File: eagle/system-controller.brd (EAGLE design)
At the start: 99 x 100 mm, 222 parts, among them IC1 TS4100, Q1 MOSFET-P-N-PAIR, Q10 MOSFET-P-N-PAIR, Q11 MOSFET-P-N-PAIR, Q12 MOSFET-P-N-PAIR, Q13 MOSFET-P-N-PAIR, Q14 MOSFET-P-N-PAIR, Q15 MOSFET-P-N-PAIR, Q16 MOSFET-P-N-PAIR, Q17 MOSFET-P-N-PAIR, Q18 MOSFET-P-N-PAIR, Q19 MOSFET-P-N-PAIR, Q2 MOSFET-P-N-PAIR, Q3 DNP/NTR4101P, Q4 DNP/NTR4101P, Q5 DNP/NTR4101P, Q6 DNP/NTR4101P, Q7 MOSFET-P-N-PAIR, Q8 MOSFET-P-N-PAIR, Q9 MOSFET-P-N-PAIR, SW1 TPS25944LRVCRWQFN-20-3X4, SW2 TPS25944LRVCRWQFN-20-3X4, SW3 TPS25944LRVCRWQFN-20-3X4, SW4 TPS25944LRVCRWQFN-20-3X4, SW5 TPS25944LRVCRWQFN-20-3X4, SW6 TPS25944LRVCRWQFN-20-3X4, SW7 TPS25944LRVCRWQFN-20-3X4, SW8 TPS25944LRVCRWQFN-20-3X4, U1 MEGA128-A, X1 8 MHz CRYSTAL-ABRACON-ABM3-SMD

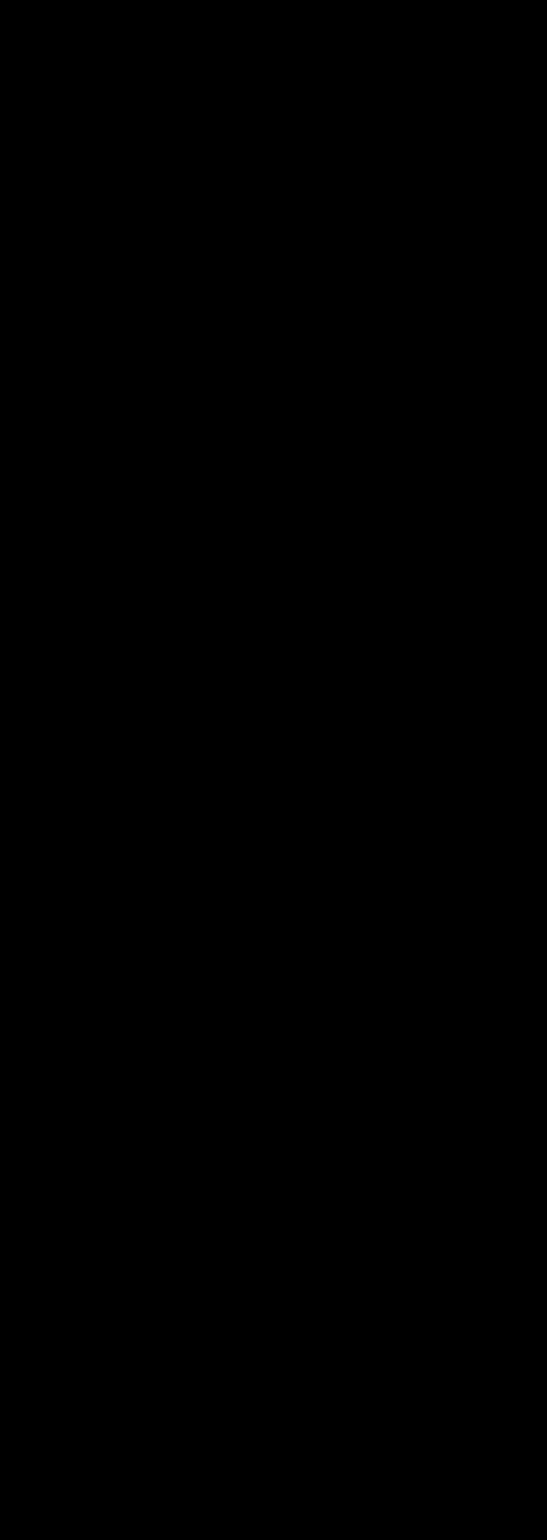
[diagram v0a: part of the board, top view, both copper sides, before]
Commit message: added the remaining test points
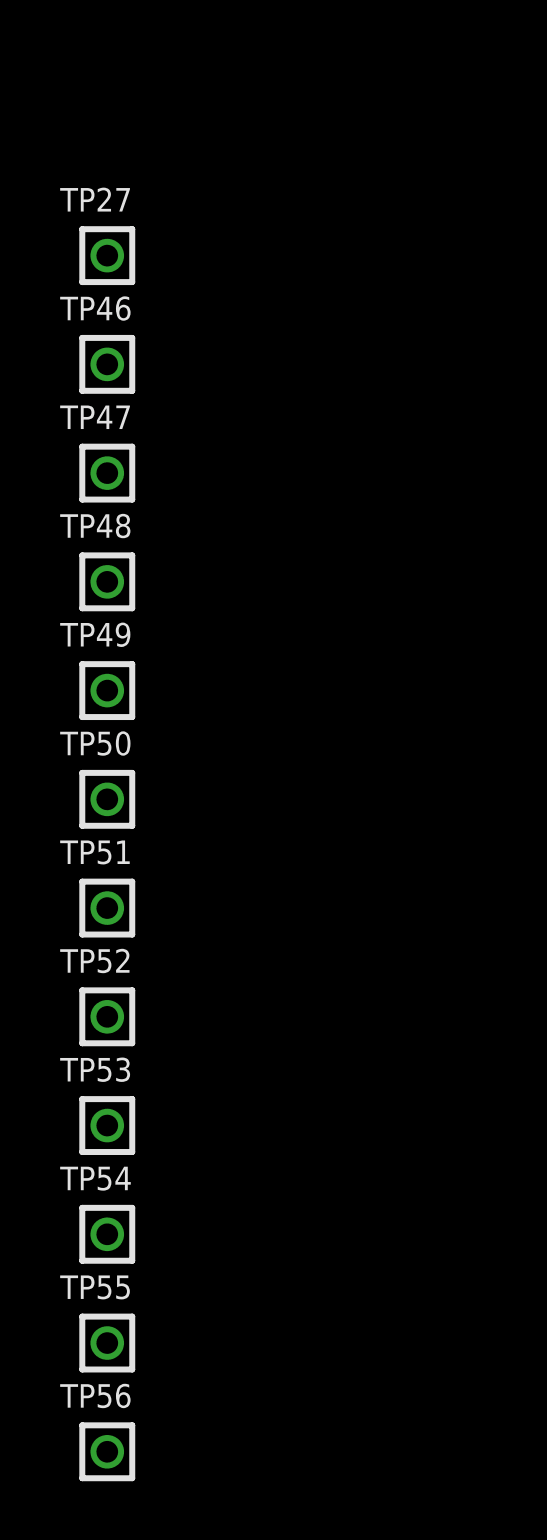
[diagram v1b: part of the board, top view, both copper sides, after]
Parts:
- added TP27, TP46, TP47, TP48, TP49, TP50, TP51, TP52, TP53, TP54, TP55, TP56: TEST-POINT, Tova:2MM-TEST-POINT
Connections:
- net N$104: now also TP56.1
- net N$27: now also TP46.1
- net N$28: now also TP27.1
- net N$34: now also TP47.1
- net N$35: now also TP49.1
- net N$37: now also TP48.1
- net N$39: now also TP55.1
- net N$40: now also TP54.1
- net N$41: now also TP53.1
- net N$42: now also TP52.1
- net N$43: now also TP51.1
- net N$44: now also TP50.1
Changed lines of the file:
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@@
 <?xml version="1.0" encoding="utf-8"?>
 <!DOCTYPE eagle SYSTEM "eagle.dtd">
-<eagle version="7.3.0">
+<eagle version="7.5.0">
 <drawing>
 <settings>
@@
 <attribute name="DPN" value="SSC53L-E3/57TGICT-ND" x="102.4" y="-12" size="1.778" layer="27" display="off"/>
 </element>
+<element name="TP27" library="Tova" package="2MM-TEST-POINT" value="TEST-POINT" x="-6.7" y="-19.3"/>
+<element name="TP46" library="Tova" package="2MM-TEST-POINT" value="TEST-POINT" x="-6.7" y="-23"/>
+<element name="TP47" library="Tova" package="2MM-TEST-POINT" value="TEST-POINT" x="-6.7" y="-26.7"/>
+<element name="TP48" library="Tova" package="2MM-TEST-POINT" value="TEST-POINT" x="-6.7" y="-30.4"/>
+<element name="TP49" library="Tova" package="2MM-TEST-POINT" value="TEST-POINT" x="-6.7" y="-34.1"/>
+<element name="TP50" library="Tova" package="2MM-TEST-POINT" value="TEST-POINT" x="-6.7" y="-37.8"/>
+<element name="TP51" library="Tova" package="2MM-TEST-POINT" value="TEST-POINT" x="-6.7" y="-41.5"/>
+<element name="TP52" library="Tova" package="2MM-TEST-POINT" value="TEST-POINT" x="-6.7" y="-45.2"/>
+<element name="TP53" library="Tova" package="2MM-TEST-POINT" value="TEST-POINT" x="-6.7" y="-48.9"/>
+<element name="TP54" library="Tova" package="2MM-TEST-POINT" value="TEST-POINT" x="-6.7" y="-52.6"/>
+<element name="TP55" library="Tova" package="2MM-TEST-POINT" value="TEST-POINT" x="-6.7" y="-56.3"/>
+<element name="TP56" library="Tova" package="2MM-TEST-POINT" value="TEST-POINT" x="-6.7" y="-60"/>
 </elements>
 <signals>
@@
 <signal name="N$27">
 <contactref element="U1" pad="18"/>
+<contactref element="TP46" pad="1"/>
+<wire x1="-6.7" y1="-23" x2="47.21" y2="43.99" width="0" layer="19" extent="1-1"/>
 </signal>
 <signal name="N$28">
 <contactref element="U1" pad="19"/>
+<contactref element="TP27" pad="1"/>
+<wire x1="-6.7" y1="-19.3" x2="48.01" y2="43.99" width="0" layer="19" extent="1-1"/>
 </signal>
 <signal name="NUCLEAROPTION2">
@@
 <signal name="N$34">
 <contactref element="U1" pad="58"/>
+<contactref element="TP47" pad="1"/>
+<wire x1="-6.7" y1="-26.7" x2="51.21" y2="59.59" width="0" layer="19" extent="1-1"/>
 </signal>
 <signal name="N$35">
 <contactref element="U1" pad="59"/>
+<contactref element="TP49" pad="1"/>
+<wire x1="-6.7" y1="-34.1" x2="50.41" y2="59.59" width="0" layer="19" extent="1-1"/>
 </signal>
 <signal name="N$37">
 <contactref element="U1" pad="60"/>
+<contactref element="TP48" pad="1"/>
+<wire x1="-6.7" y1="-30.4" x2="49.61" y2="59.59" width="0" layer="19" extent="1-1"/>
 </signal>
 <signal name="N$39">
 <contactref element="U1" pad="4"/>
+<contactref element="TP55" pad="1"/>
+<wire x1="-6.7" y1="-56.3" x2="44.61" y2="55.39" width="0" layer="19" extent="1-1"/>
 </signal>
 <signal name="N$40">
 <contactref element="U1" pad="5"/>
+<contactref element="TP54" pad="1"/>
+<wire x1="-6.7" y1="-52.6" x2="44.61" y2="54.59" width="0" layer="19" extent="1-1"/>
 </signal>
 <signal name="N$41">
 <contactref element="U1" pad="6"/>
+<contactref element="TP53" pad="1"/>
+<wire x1="-6.7" y1="-48.9" x2="44.61" y2="53.79" width="0" layer="19" extent="1-1"/>
 </signal>
 <signal name="N$42">
 <contactref element="U1" pad="7"/>
+<contactref element="TP52" pad="1"/>
+<wire x1="-6.7" y1="-45.2" x2="44.61" y2="52.99" width="0" layer="19" extent="1-1"/>
 </signal>
 <signal name="N$43">
 <contactref element="U1" pad="8"/>
+<contactref element="TP51" pad="1"/>
+<wire x1="-6.7" y1="-41.5" x2="44.61" y2="52.19" width="0" layer="19" extent="1-1"/>
 </signal>
 <signal name="N$44">
 <contactref element="U1" pad="9"/>
+<contactref element="TP50" pad="1"/>
+<wire x1="-6.7" y1="-37.8" x2="44.61" y2="51.39" width="0" layer="19" extent="1-1"/>
 </signal>
 <signal name="N$46">
@@
 <signal name="N$104">
 <contactref element="U1" pad="32"/>
+<contactref element="TP56" pad="1"/>
+<wire x1="-6.7" y1="-60" x2="58.41" y2="43.99" width="0" layer="19" extent="1-1"/>
 </signal>
 </signals>

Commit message: working on board layout. Have everything organized in in general location. Working on routing.
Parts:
- removed C10, C18, C20, C22, C24, C31, R52, R64, R65, R66, RILIM, RIMON: TBD, rcl_custom:.0603-B-NOSILK
- removed C19, C21, C23, C29: 1uF, rcl_custom:.0603-B-NOSILK
- removed C40: 10nF, rcl_custom:.0603-B-NOSILK
- removed LED13, LED14, LED15: DNP/AMB, psas_c3_team05:LED-0603
- removed LED8: GRN, psas_c3_team05:LED-0603
- removed Q14, Q15, Q16, Q17, Q18, Q19, Q8: MOSFET-P-N-PAIR, ic-transistor-mosfet-n-p:SOT23-6
- removed Q20: (no value), adafruit:SOT23
- removed R11, R17, R48, R49, R50, R54, R55, R57, R58, R59, R60, R62: 47k, rcl_custom:.0603-B-NOSILK
- removed R47, R53: 4.7k, rcl_custom:.0603-B-NOSILK
- removed R51, R56, R67: 1k, rcl_custom:.0603-B-NOSILK
- removed R63: 390, rcl_custom:.0603-B-NOSILK
- removed RUVLO1, RUVLO2, RUVLO3, RUVLO4, RUVLO5, RUVLO6, RUVLO7, RUVLO8: 93.1k, rcl_custom:.0603-B-NOSILK
- removed SW8: TPS25944LRVCRWQFN-20-3X4, WQFN-20-3x4:QFN-20-L
- removed TP1: TPSPAD1-13, testpad:P1-13
- removed TP28, TP29, TP30, TP31, TP32, TP33, TP34, TP35, TP36, TP37, TP38, TP39, TP40, TP41, TP42, TP5: TEST-POINT, Tova:2MM-TEST-POINT
- added CFUSE3A, CFUSE7A, CLDO1: 1uF, rcl_custom:.0603-B-NOSILK
- added CFUSE7, CHWWD, RHWWD0, RHWWD1, RHWWD2, RHWWD4, RILIM0, RIMON0: TBD, rcl_custom:.0603-B-NOSILK
- added CLDO2: 10nF, rcl_custom:.0603-B-NOSILK
- added CLDO3: 2.2uF, rcl_custom:.0603-B-NOSILK
- added CPHOTO0A, CPHOTO1B, CPHOTO3A, CPHOTO3B: 100nF, rcl_custom:.0603-B-NOSILK
- added LED0, LED3, LED4, LED5: GRN, psas_c3_team05:LED-0603
- added Q0: MOSFET-P-N-PAIR, ic-transistor-mosfet-n-p:SOT23-6
- added R0/UVLO, R1/UVLO, R2/UVLO, R3/UVLO, R4/UVLO, R5/UVLO, R6/UVLO, R7/UVLO, RA1, RA2, RA3, RA4, RA5, RA6, RA7, RA8: 47k, rcl_custom:.0603-B-NOSILK
- added RHWWD3: 1k, rcl_custom:.0603-B-NOSILK
- added RLDO1: 10k, rcl_custom:.0603-B-NOSILK
- added RPHOTO0A, RPHOTO0B, RPHOTO1A, RPHOTO1B, RPHOTO2A, RPHOTO2B, RPHOTO3A, RPHOTO3B: 390, rcl_custom:.0603-B-NOSILK
- added SW0: TPS25944LRVCRWQFN-20-3X4, WQFN-20-3x4:QFN-20-L
- added TP0GHT, TP0GOOD, TP1GHT, TP1GOOD, TP2GHT, TP2GOOD, TP3GHT, TP3GOOD, TP4GHT, TP4GOOD, TP5GHT, TP5GOOD, TP6GHT, TP6GOOD, TP7GHT, TP7GOOD, TPLDOA: TEST-POINT, Tova:2MM-TEST-POINT
- C11, C13, C15, C17, C9: value 1uF -> TBD
- C12, C14, C16: value TBD -> 1uF
- C2, C6: value 100nF -> 1uF
- C3, C5: value 100nF -> TBD
- C4: value 2.2uF -> 1uF
- LED10, LED11, LED12, LED9: value GRN -> DNP/AMB
- LED6: value DNP/AMB -> GRN
- Q10, Q11, Q12, Q9: value MOSFET-P-N-PAIR -> DNP/NTR4101P; device ic-transistor-mosfet-n-p:SOT23-6 -> Tova:SOT23
- Q13: value MOSFET-P-N-PAIR -> (none); device ic-transistor-mosfet-n-p:SOT23-6 -> adafruit:SOT23
- Q3, Q4, Q5, Q6: value DNP/NTR4101P -> MOSFET-P-N-PAIR; device Tova:SOT23 -> ic-transistor-mosfet-n-p:SOT23-6
- R1, R3, R7: value 390 -> 47k
- R10, R5: value 390 -> 93.1k
- R12: value 10k -> 1k
- R14, R20, R28, R33, R38, R43: value 47k -> 4.7k
- R15, R21: value 1k -> 47k
- R16, R25: value 47k -> 93.1k
- R18: value 4.7k -> 1k
- R2, R8: value 390 -> 4.7k
- R26, R31, R36, R41, R46, R6: value 47k -> 1k
- R27, R32, R37, R42, R9: value 4.7k -> 47k
- R30, R35, R40, R45: value 1k -> 93.1k
- moved TP14 157.3 mm to (7.50, 21.5), turned to 270 degrees
- moved TP13 153.2 mm to (7.50, 19.0), turned to 270 degrees
- moved TP12 149.1 mm to (7.50, 16.5), turned to 270 degrees
- moved TP11 145.1 mm to (7.50, 14.0), turned to 270 degrees
- moved TP10 141.1 mm to (7.50, 11.5), turned to 270 degrees
- moved TP6 126.3 mm to (19.0, 13.0), turned to 180 degrees
- moved R6 121.9 mm to (81.0, 86.5), turned to 270 degrees
- moved TP3 120.1 mm to (21.5, 13.0), turned to 0 degrees
- moved TP2 114.5 mm to (23.5, 13.0), turned to 0 degrees
- moved D3 108.8 mm to (27.1, 66.6), turned to 90 degrees
- moved R16 104.5 mm to (88.0, 65.0), turned to 270 degrees
- moved TP44 104.1 mm to (28.0, 87.4), turned to 0 degrees
- moved TP19 102.7 mm to (40.0, 38.0), turned to 0 degrees
- moved TP26 100.3 mm to (7.50, 24.0), turned to 270 degrees
- moved TP56 98.8 mm to (18.5, 35.5), turned to 180 degrees
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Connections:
- removed net N$31: C10.1, SW1.18
- removed net N$7: Q2.3, Q2.6, R14.2
- new net C10\: CFUSE3A.2, Q3.2, R19.1, SW3.10, SW3.11, SW3.12, SW3.13, SW3.9
- new net INOF: C3.1, SW0.18
- new net N$110: Q7.4, R45.1
- new net N$111: Q6.4, R40.1
- net 3V: now also CLDO3.1, CPHOTO1B.2, CPHOTO3B.2, Q10.2, Q11.2, Q12.2, Q9.2, RA1.1, RA2.1, RA3.1, RA4.1, RA5.1, RA6.1, RA7.1, RA8.1, U$2.5; no longer C2.2, C4.1, C6.2, Q3.2, Q4.2, Q5.2, Q6.2, R11.1, R17.1, R50.1, R57.1, R58.1, R59.1, R60.1, R62.1, U$3.5
- net GND: now also C11.2, C12.1, C13.2, C14.1, C15.2, C16.1, C17.2, C3.2, C4.1, C5.2, C9.2, CFUSE3A.1, CFUSE7.2, CFUSE7A.1, CHWWD.2, CLDO1.1, CLDO2.2, CLDO3.2, CPHOTO0A.1, CPHOTO1B.1, CPHOTO3A.1, CPHOTO3B.1, LED0.K, LED3.K, LED4.K, LED5.K, Q0.5, Q13.2, Q3.5, Q4.5, Q5.5, Q6.5, R0/UVLO.2, R1/UVLO.2, R15.2, R2/UVLO.2, R21.2, R29.2, R3.2, R3/UVLO.2, R34.2, R39.2, R4/UVLO.2, R44.2, R5/UVLO.2, R6/UVLO.2, R7/UVLO.2, R9.2, RHWWD3.2, RHWWD4.2, RILIM0.2, RIMON0.2, SW0.1, SW0.15, SW0.16, SW0.21, SW0.3, TP0GHT.1, TP1GHT.1, TP2GHT.1, TP3GHT.1, TP4GHT.1, TP5GHT.1, TP6GHT.1, TP7GHT.1; no longer C10.2, C11.1, C12.2, C13.1, C14.2, C15.1, C16.2, C17.1, C18.2, C19.1, C20.2, C21.1, C22.2, C23.1, C24.2, C29.1, C3.1, C31.2, C4.2, C40.2, C5.1, C9.1, LED13.K, LED14.K, LED15.K, LED8.K, Q10.5, Q11.5, Q12.5, Q20.2, Q8.5, Q9.5, R13.2, R16.2, R19.2, R25.2, R26.2, R28.2, R31.2, R33.2, R36.2, R38.2, R41.2, R43.2, R46.2, R48.2, R54.2, R6.2, R66.2, R67.2, RILIM.2, RIMON.2, SW8.1, SW8.15, SW8.16, SW8.21, SW8.3, TP28.1, TP30.1, TP32.1, TP34.1, TP36.1, TP38.1, TP40.1, TP42.1
- net N$10: now also R16.2, R2/UVLO.1, SW2.14; no longer R41.1, RUVLO2.2, SW3.14
- net N$100: now also RILIM6.1, SW6.17; no longer RILIM7.1, SW8.17
- net N$101: now also SW6.2, TP6GOOD.1; no longer SW8.2, TP39.1
- net N$102: now also C17.1, SW6.18; no longer C24.1, SW8.18
- net N$103: now also Q6.1, R38.2, R39.1; no longer Q11.1, R19.1, R47.2
- net N$105: now also Q6.3, Q6.6, R37.2; no longer Q11.6, Q18.3, R49.2
- net N$106: now also CHWWD.1, Q13.1, RHWWD4.1; no longer C31.1, Q20.1, R66.1
- net N$108: now also Q5.4, R35.1; no longer Q19.4, RUVLO8.1
- net N$109: now also RHWWD0.1, RHWWD1.1, RHWWD2.1, RHWWD3.1; no longer R52.1, R64.1, R65.1, R67.1
- net N$16: now also RPHOTO2A.2, U$3.4; no longer R1.2, U$2.4
- net N$18: now also RPHOTO3B.1; no longer R8.1
- net N$19: now also SW2.17; no longer SW3.17
- net N$2: now also Q1.4, R10.1; no longer Q2.1, R54.1, R9.2
- net N$20: now also RPHOTO3A.2; no longer R7.2
- net N$21: now also RILIM0.1, SW0.17; no longer RILIM.1, SW1.17
- net N$22: now also RLDO1.2, TPLDOA.1; no longer R12.2, TP1.TP
- net N$23: now also CLDO2.1; no longer C40.1
- net N$24: now also RPHOTO1B.2, U$2.4; no longer R63.2, U$3.4
- net N$25: now also SW0.2, TP0GOOD.1; no longer SW1.2, TP5.1
- net N$26: now also LED0.A, R6.2; no longer LED1.A, R15.2
- net N$29: now also R1/UVLO.1, R10.2, SW1.14; no longer R46.1, RUVLO1.2, SW2.14
- net N$3: now also R0/UVLO.1, R5.2; no longer Q13.4, RUVLO1.1
- net N$30: now also SW1.17; no longer SW2.17
- net N$32: now also SW1.2, TP1GOOD.1; no longer SW2.2, TP29.1
- net N$38: now also C5.1, SW1.18; no longer C12.1, SW2.18
- net N$4: now also RPHOTO2B.1, U$3.1; no longer R10.1, U$2.1
- net N$45: now also LED1.A, R12.2; no longer LED2.A, R21.2
- net N$49: now also R8.2, R9.1; no longer R18.2, R48.1
- net N$5: now also RPHOTO0A.2; no longer R2.2
- net N$50: now also Q0.1, R3.1; no longer Q14.4, RUVLO2.1
- net N$51: now also Q1.3, R7.2; no longer Q13.3, R20.2
- net N$52: now also LED2.A, R18.2; no longer LED7.A, R30.2
- net N$53: now also LED12.A; no longer LED15.A
- net N$54: now also Q11.3; no longer Q4.3
- net N$55: now also Q12.3; no longer Q3.3
- net N$56: now also LED11.A; no longer LED14.A
- net N$57: now also LED9.A; no longer LED6.A
- net N$58: now also Q9.3; no longer Q6.3
- net N$59: now also SW2.2, TP2GOOD.1; no longer SW3.2, TP31.1
- net N$6: now also RPHOTO0B.1; no longer R3.1
- net N$60: now also LED10.A; no longer LED13.A
- net N$61: now also Q10.3; no longer Q5.3
- net N$62: now also C9.1, SW2.18; no longer C14.1, SW3.18
- net N$63: now also Q2.1, R14.2, R15.1; no longer Q7.1, R27.2, R43.1
- net N$64: now also R16.1; no longer RUVLO3.1
- net N$65: now also Q2.3, Q2.6, R13.2; no longer Q14.3, Q7.6, R29.2
- net N$66: now also LED3.A, R26.2; no longer LED8.A, R35.2
- net N$67: now also R45.2, R7/UVLO.1, SW7.14; no longer R16.1, RUVLO8.2, SW4.14
- net N$68: now also RILIM7.1, SW7.17; no longer RILIM3.1, SW4.17
- net N$69: now also SW7.2, TP7GOOD.1; no longer SW4.2, TP41.1
- net N$70: now also CFUSE7.1, SW7.18; no longer C16.1, SW4.18
- net N$71: now also Q7.1, R43.2, R44.1; no longer Q12.1, R13.1, R53.2
- net N$72: now also Q0.3, Q0.6, R1.2; no longer Q15.4, RUVLO4.1
- net N$73: now also Q7.3, Q7.6, R42.2; no longer Q12.6, Q19.3, R55.2
- net N$74: now also LED4.A, R31.2; no longer LED9.A, R40.2
- net N$75: now also R35.2, R5/UVLO.1; no longer R26.1, RUVLO6.2
- net N$76: now also RILIM5.1; no longer RILIM4.1
- net N$77: now also TP5GOOD.1; no longer TP37.1
- net N$78: now also C15.1; no longer C18.1
- net N$79: now also Q5.1, R33.2, R34.1; no longer Q10.1, R28.1, R42.2
- net N$8: now also RPHOTO1A.2, U$2.1; no longer R5.2, U$3.1
- net N$80: now also Q0.4, R5.1; no longer Q16.4, RUVLO5.1
- net N$81: now also Q5.3, Q5.6, R32.2; no longer Q10.6, Q17.3, R44.2
- net N$82: now also LED5.A, R36.2; no longer LED10.A, R45.2
- net N$83: now also R30.2, R4/UVLO.1, SW4.14; no longer R31.1, RUVLO5.2, SW6.14
- net N$84: now also RILIM4.1, SW4.17; no longer RILIM5.1, SW6.17
- net N$85: now also SW4.2, TP4GOOD.1; no longer SW6.2, TP35.1
- net N$86: now also C13.1, SW4.18; no longer C20.1, SW6.18
- net N$87: now also Q4.1, R28.2, R29.1; no longer Q9.1, R33.1, R37.2
- net N$88: now also Q3.4, R25.1; no longer Q17.4, RUVLO6.1
- net N$89: now also Q4.3, Q4.6, R27.2; no longer Q16.3, Q9.6, R39.2
- net N$9: now also SW0.14; no longer R6.1, RUVLO3.2, SW1.14
- net N$90: now also LED6.A, R41.2; no longer LED11.A, R51.2
- net N$91: now also R25.2, R3/UVLO.1, SW3.14; no longer R36.1, RUVLO4.2, SW7.14
- net N$92: now also RILIM3.1, SW3.17; no longer RILIM6.1, SW7.17
- net N$93: now also SW3.2, TP3GOOD.1; no longer SW7.2, TP33.1
- net N$94: now also C11.1, SW3.18; no longer C22.1, SW7.18
- net N$95: now also Q3.1, R20.2, R21.1; no longer Q8.1, R32.2, R38.1
- net N$96: now also Q4.4, R30.1; no longer Q18.4, RUVLO7.1
- net N$97: now also Q3.3, Q3.6, R19.2; no longer Q15.3, Q8.6, R34.2
- net N$98: now also LED7.A, R46.2; no longer LED12.A, R56.2
- net N$99: now also R40.2, R6/UVLO.1, SW6.14; no longer R25.1, RUVLO7.2, SW8.14
- net NUCLEAROPTION0: now also RHWWD2.2; no longer R65.2
- net NUCLEAROPTION1: now also RHWWD1.2; no longer R64.2
- net NUCLEAROPTION2: now also RHWWD0.2; no longer R52.2
- net NUCLEAROPTION_OUT: now also Q13.3; no longer Q20.3
- net PCB3_EN: now also R20.1; no longer R32.1
- net RXD0: now also Q12.1, RPHOTO3B.2; no longer Q3.1, R8.2
- net RXD1: now also Q10.1, RPHOTO1B.1; no longer Q5.1, R63.1
- net TXD0: now also Q11.1, RPHOTO2B.2; no longer Q4.1, R10.2
- net TXD1: now also Q9.1, RPHOTO0B.2; no longer Q6.1, R3.2
- net UART_FC_RX: now also RPHOTO0A.1; no longer R2.1
- net UART_FC_TX: now also RPHOTO1A.1; no longer R5.1
- net UART_FC_VCC: now also CPHOTO0A.2; no longer C5.2
- net UART_LGR_RX: now also RPHOTO2A.1; no longer R1.1
- net UART_LGR_TX: now also RPHOTO3A.1; no longer R7.1
- net UART_LGR_VCC: now also CPHOTO3A.2, U$3.5; no longer C3.2, U$2.5
- net V+: now also CLDO1.2, RLDO1.1; no longer C23.2, R12.1
- net VBC1: now also R12.1, SW1.4, SW1.5, SW1.6, SW1.7, SW1.8; no longer R21.1, SW2.4, SW2.5, SW2.6, SW2.7, SW2.8
- net VBC2: now also R18.1, SW2.4, SW2.5, SW2.6, SW2.7, SW2.8; no longer R30.1, SW3.4, SW3.5, SW3.6, SW3.7, SW3.8
- net VBC4: now also R31.1, SW4.4, SW4.5, SW4.6, SW4.7, SW4.8; no longer R40.1, SW6.4, SW6.5, SW6.6, SW6.7, SW6.8
- net VBC5: now also R36.1; no longer R45.1
- net VBC6: now also R41.1, SW6.4, SW6.5, SW6.6, SW6.7, SW6.8; no longer R51.1, SW8.4, SW8.5, SW8.6, SW8.7, SW8.8
- net VBC7: now also R46.1, SW7.4, SW7.5, SW7.6, SW7.7, SW7.8; no longer R56.1, SW4.4, SW4.5, SW4.6, SW4.7, SW4.8
- net VBUS: now also C12.2, C14.2, C16.2, C2.2, C4.2, C6.2, CFUSE7A.2, Q0.2, Q1.2, Q4.2, Q5.2, Q6.2, Q7.2, R1.1, R13.1, R27.1, R32.1, R37.1, R42.1, R7.1; no longer C11.2, C13.2, C15.2, C17.2, C19.2, C21.2, C29.2, C9.2, Q13.2, Q14.2, Q15.2, Q16.2, Q17.2, Q18.2, Q19.2, R14.1, R20.1, R29.1, R34.1, R39.1, R44.1, R49.1, R55.1, SW3.10, SW3.11, SW3.12, SW3.13, SW3.9, SW8.10, SW8.11, SW8.12, SW8.13, SW8.9
- net VCB0: now also R6.1, SW0.4, SW0.5, SW0.6, SW0.7, SW0.8; no longer R15.1, SW1.4, SW1.5, SW1.6, SW1.7, SW1.8
- net VCB0_!FLT: now also RA1.2, SW0.20; no longer R50.2, SW1.20
- net VCB0_EN: now also R2.1; no longer R9.1
- net VCB0_IMON: now also RIMON0.1, SW0.19; no longer RIMON.1, SW1.19
- net VCB1_!FLT: now also RA2.2, SW1.20; no longer R17.2, SW2.20
- net VCB1_EN: now also R8.1; no longer R18.1
- net VCB1_IMON: now also SW1.19; no longer SW2.19
- net VCB2_!FLT: now also RA3.2, SW2.20; no longer R57.2, SW3.20
- net VCB2_EN: now also R14.1; no longer R27.1
- net VCB2_IMON: now also SW2.19; no longer SW3.19
- net VCB3: now also R26.1, SW3.4, SW3.5, SW3.6, SW3.7, SW3.8; no longer R35.1, SW7.4, SW7.5, SW7.6, SW7.7, SW7.8
- net VCB3_!FLT: now also RA4.2, SW3.20; no longer R11.2, SW7.20
- net VCB3_IMON: now also RIMON3.1, SW3.19; no longer RIMON6.1, SW7.19
- net VCB4_!FLT: now also RA5.2, SW4.20; no longer R58.2, SW6.20
- net VCB4_EN: now also R28.1; no longer R37.1
- net VCB4_IMON: now also RIMON4.1, SW4.19; no longer RIMON5.1, SW6.19
- net VCB5_!FLT: now also RA6.2; no longer R62.2
- net VCB5_EN: now also R33.1; no longer R42.1
- net VCB5_IMON: now also RIMON5.1; no longer RIMON4.1
- net VCB6_!FLT: now also RA7.2, SW6.20; no longer R59.2, SW8.20
- net VCB6_EN: now also R38.1; no longer R47.1
- net VCB6_IMON: now also RIMON6.1, SW6.19; no longer RIMON7.1, SW8.19
- net VCB7_!FLT: now also RA8.2, SW7.20; no longer R60.2, SW4.20
- net VCB7_EN: now also R43.1; no longer R53.1
- net VCB7_IMON: now also RIMON7.1, SW7.19; no longer RIMON3.1, SW4.19
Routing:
- net VBC7: track 0.00 -> 91.6 mm
- net VBC6: track 0.00 -> 80.5 mm
- net VBUS: track 0.00 -> 73.8 mm
- net VBC5: track 0.00 -> 73.6 mm
- net VBC4: track 0.00 -> 62.5 mm
- net VCB3: track 0.00 -> 51.0 mm
- net 3V: track 0.00 -> 43.2 mm
- net VBC2: track 0.00 -> 39.9 mm
- net VBC1: track 0.00 -> 28.8 mm
- net VCB0: track 0.00 -> 20.3 mm
- net VCB7_!FLT: track 0.00 -> 19.2 mm
- net PB6: track 0.00 -> 18.3 mm
- net VCB6_!FLT: track 0.00 -> 18.2 mm
- net PB5: track 0.00 -> 17.6 mm
- net VCB5_!FLT: track 0.00 -> 17.5 mm
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
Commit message: Pushing newest changes to the board layout
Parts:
- moved R61 93.3 mm to (17.9, 83.1), turned to 270 degrees
- moved R24 86.4 mm to (18.0, 71.1), turned to 270 degrees
- moved R22 81.0 mm to (18.0, 59.1)
- moved R23 77.9 mm to (18.0, 48.1)
- moved C27 32.7 mm to (32.4, 14.4), turned to 90 degrees
- moved C28 30.0 mm to (34.2, 14.4), turned to 90 degrees
- moved CLDO1 21.9 mm to (51.4, 69.9), turned to 90 degrees
- moved RLDO1 18.8 mm to (49.5, 69.9), turned to 270 degrees
- moved C25 18.3 mm to (42.0, 57.0), turned to 0 degrees
- moved RIMON4 16.0 mm to (42.0, 55.0), turned to 180 degrees
- moved RIMON3 15.9 mm to (49.0, 61.0)
- moved RIMON1 15.8 mm to (45.0, 61.0)
- moved U$8 15.8 mm to (45.6, 70.3), turned to 0 degrees
- moved RIMON0 15.6 mm to (47.0, 61.0)
- moved RIMON7 15.1 mm to (46.9, 51.0), turned to 270 degrees
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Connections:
- removed net C10\: CFUSE3A.2, Q3.2, R19.1, SW3.10, SW3.11, SW3.12, SW3.13, SW3.9
- removed net N$3: R0/UVLO.1, R5.2
- new net GMD: LED0.K
- net GND: no longer LED0.K
- net N$9: now also R0/UVLO.1, R5.2
- net VBUS: now also CFUSE3A.2, Q3.2, R19.1, SW0.10, SW0.11, SW0.12, SW0.13, SW0.9, SW3.10, SW3.11, SW3.12, SW3.13, SW3.9
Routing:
- net VCB0_!FLT: track 14.5 -> 157.4 mm, vias 0 -> 4
- net N$49: track 5.83 -> 145.1 mm, vias 0 -> 4
- net N$63: track 5.84 -> 140.8 mm, vias 0 -> 4
- net VCB1_!FLT: track 14.7 -> 143.9 mm, vias 0 -> 4
- net N$95: track 5.83 -> 134.8 mm, vias 0 -> 4
- net N$57: track 0.00 -> 128.5 mm, vias 0 -> 2
- net VCB2_!FLT: track 15.3 -> 133.9 mm, vias 0 -> 2
- net N$60: track 0.00 -> 118.3 mm, vias 0 -> 2
- net N$26: track 0.00 -> 114.8 mm, vias 0 -> 2
- net N$87: track 5.83 -> 118.8 mm, vias 0 -> 4
- net N$56: track 0.00 -> 109.2 mm, vias 0 -> 2
- net N$79: track 5.83 -> 109.5 mm, vias 0 -> 4
- net N$45: track 0.00 -> 101.6 mm, vias 0 -> 2
- net N$53: track 0.00 -> 98.2 mm, vias 0 -> 2
- net VCB3_!FLT: track 16.1 -> 111.6 mm, vias 0 -> 2
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- added copper zone on layer 15, net 3V
- added copper zone on layer 15, net V+
- added copper zone on layer 15, net VBUS
- added copper zone on layer 15, net VSOL
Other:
- board text added: "Note: Look for hidden air wires"

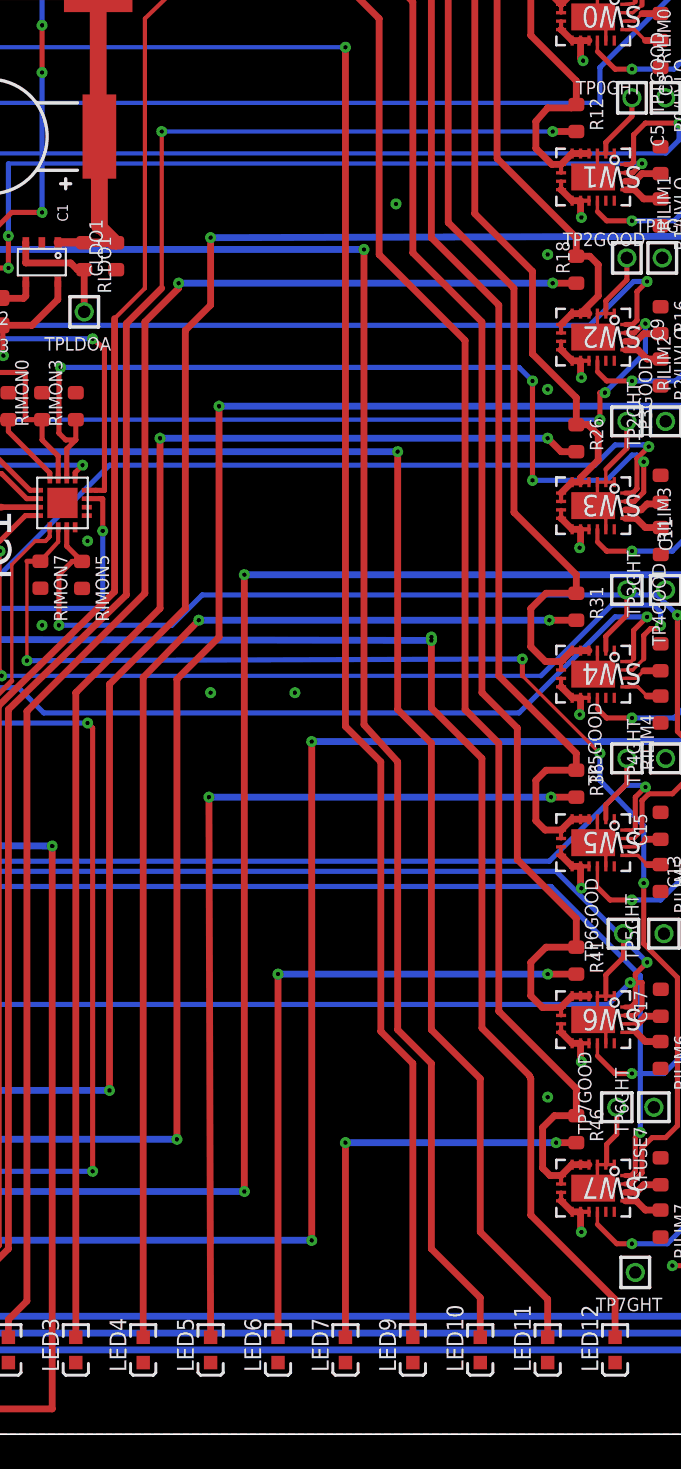
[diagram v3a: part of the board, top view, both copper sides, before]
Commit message: Design review with Shan and Andrew. Cleaned up polygons and polygon ranks. Used correct DRC rules.
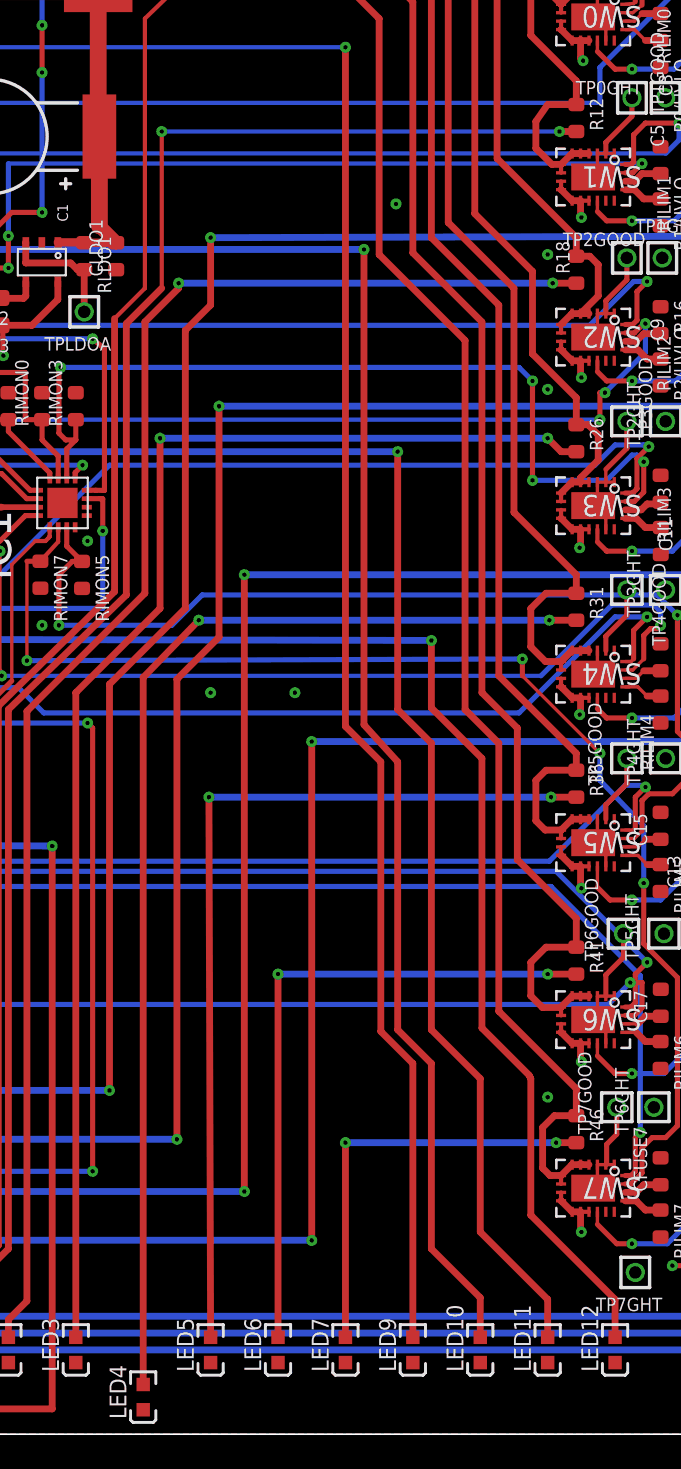
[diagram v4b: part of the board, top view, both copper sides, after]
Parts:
- moved LED4 2.80 mm to (53.0, 2.20)
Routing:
- net N$74: track 66.3 -> 69.1 mm
- removed copper zone on layer 15, net V+
- removed copper zone on layer 15, net VSOL
